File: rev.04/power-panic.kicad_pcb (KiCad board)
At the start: 2 copper layers, 40 x 26 mm, 27 parts, among them P1 PE, P10 AC, P3 N, P5 L, P7 24V, P8 AC_FAULT, P9 measure, Q1 MMBF170LT1G, Q2 MMBF170LT1G, U1 LTV-354T_

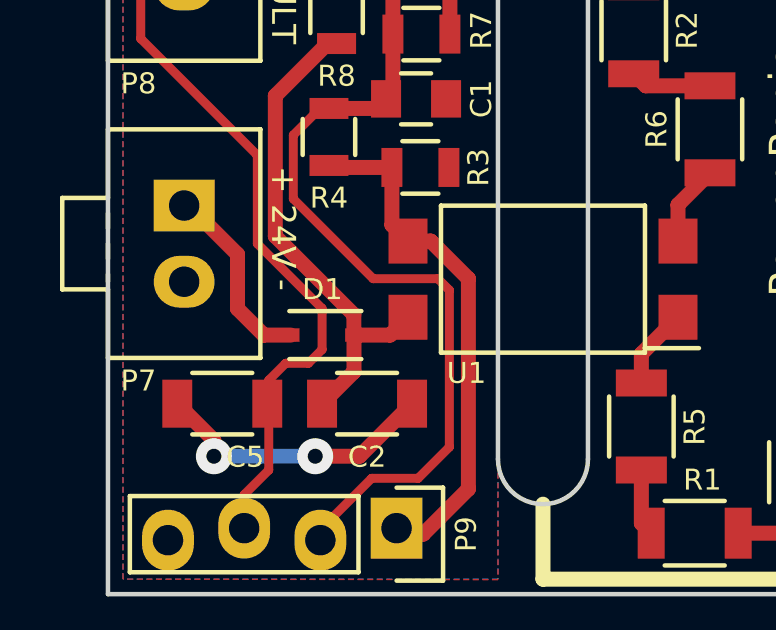
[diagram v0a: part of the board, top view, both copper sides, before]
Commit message: Begin work of reassociating footprints
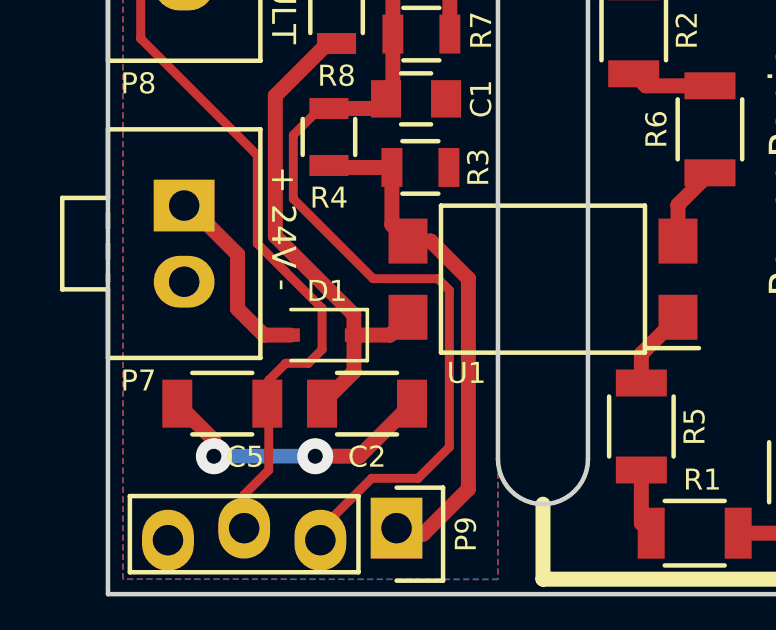
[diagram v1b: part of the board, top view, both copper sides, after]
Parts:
- D1: footprint Diodes_SMD:SOD-323 -> Diodes_SMD:D_SOD-323
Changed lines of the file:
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@@
-(kicad_pcb (version 4) (host pcbnew 4.0.5+dfsg1-4)
+(kicad_pcb (version 4) (host pcbnew 4.0.7)
   (general
     (links 43)
@@
     (43 Eco2.User user)
     (44 Edge.Cuts user)
-    (45 Margin user)
+    (45 Margin user hide)
     (46 B.CrtYd user)
     (47 F.CrtYd user)
@@
     (pad_to_mask_clearance 0.2)
     (aux_axis_origin 0 0)
-    (visible_elements FFFEFF7F)
+    (visible_elements 7FFFFFFF)
     (pcbplotparams
       (layerselection 0x010fc_80000001)
@@
     )
   )
-  (module Diodes_SMD:SOD-323 (layer F.Cu)
-    (at 7.146 -8.636 180)
-    (descr SOD-323)
-    (tags SOD-323)
-    (attr smd)
-    (fp_text reference D1 (at 0 1.524 180) (layer F.SilkS)
-      (effects (font (size 0.7 0.7) (thickness 0.15)))
-    )
-    (fp_text value D_ALT (at 0.1 1.9 180) (layer F.Fab)
-      (effects (font (size 1 1) (thickness 0.15)))
-    )
-    (fp_line (start 0.2 0) (end 0.45 0) (layer F.Fab) (width 0.15))
-    (fp_line (start 0.2 0.35) (end -0.3 0) (layer F.Fab) (width 0.15))
-    (fp_line (start 0.2 -0.35) (end 0.2 0.35) (layer F.Fab) (width 0.15))
-    (fp_line (start -0.3 0) (end 0.2 -0.35) (layer F.Fab) (width 0.15))
-    (fp_line (start -0.3 0) (end -0.5 0) (layer F.Fab) (width 0.15))
-    (fp_line (start -0.3 -0.35) (end -0.3 0.35) (layer F.Fab) (width 0.15))
-    (fp_line (start -0.85 0.65) (end -0.85 -0.65) (layer F.Fab) (width 0.15))
-    (fp_line (start 0.85 0.65) (end -0.85 0.65) (layer F.Fab) (width 0.15))
-    (fp_line (start 0.85 -0.65) (end 0.85 0.65) (layer F.Fab) (width 0.15))
-    (fp_line (start -0.85 -0.65) (end 0.85 -0.65) (layer F.Fab) (width 0.15))
-    (fp_line (start -1.5 -0.95) (end 1.5 -0.95) (layer F.CrtYd) (width 0.05))
-    (fp_line (start 1.5 -0.95) (end 1.5 0.95) (layer F.CrtYd) (width 0.05))
-    (fp_line (start -1.5 0.95) (end 1.5 0.95) (layer F.CrtYd) (width 0.05))
-    (fp_line (start -1.5 -0.95) (end -1.5 0.95) (layer F.CrtYd) (width 0.05))
-    (fp_line (start -1.3 0.8) (end 1.1 0.8) (layer F.SilkS) (width 0.15))
-    (fp_line (start -1.3 -0.8) (end 1.1 -0.8) (layer F.SilkS) (width 0.15))
-    (pad 1 smd rect (at -1.055 0 180) (size 0.59 0.45) (layers F.Cu F.Paste F.Mask)
-      (net 11 /+24V))
-    (pad 2 smd rect (at 1.055 0 180) (size 0.59 0.45) (layers F.Cu F.Paste F.Mask)
-      (net 8 "Net-(D1-Pad2)"))
-    (model Diodes_SMD.3dshapes/SOD-323.wrl
-      (at (xyz 0 0 0))
-      (scale (xyz 1 1 1))
-      (rotate (xyz 0 0 180))
-    )
-  )
   (module Resistors_SMD:R_1206 (layer F.Cu)
     (at 25.146 -7.62 180)
@@
     )
   )
+  (module Diodes_SMD:D_SOD-323 (layer F.Cu)
+    (at 7.146 -8.636 180)
+    (descr SOD-323)
+    (tags SOD-323)
+    (attr smd)
+    (fp_text reference D1 (at -0.154 1.464 180) (layer F.SilkS)
+      (effects (font (size 0.7 0.7) (thickness 0.15)))
+    )
+    (fp_text value D_ALT (at 0.046 1.964 180) (layer F.Fab) hide
+      (effects (font (size 1 1) (thickness 0.15)))
+    )
+    (fp_text user %R (at -0.154 1.464 180) (layer F.Fab) hide
+      (effects (font (size 1 1) (thickness 0.15)))
+    )
+    (fp_line (start -1.5 -0.85) (end -1.5 0.85) (layer F.SilkS) (width 0.12))
+    (fp_line (start 0.2 0) (end 0.45 0) (layer F.Fab) (width 0.1))
+    (fp_line (start 0.2 0.35) (end -0.3 0) (layer F.Fab) (width 0.1))
+    (fp_line (start 0.2 -0.35) (end 0.2 0.35) (layer F.Fab) (width 0.1))
+    (fp_line (start -0.3 0) (end 0.2 -0.35) (layer F.Fab) (width 0.1))
+    (fp_line (start -0.3 0) (end -0.5 0) (layer F.Fab) (width 0.1))
+    (fp_line (start -0.3 -0.35) (end -0.3 0.35) (layer F.Fab) (width 0.1))
+    (fp_line (start -0.9 0.7) (end -0.9 -0.7) (layer F.Fab) (width 0.1))
+    (fp_line (start 0.9 0.7) (end -0.9 0.7) (layer F.Fab) (width 0.1))
+    (fp_line (start 0.9 -0.7) (end 0.9 0.7) (layer F.Fab) (width 0.1))
+    (fp_line (start -0.9 -0.7) (end 0.9 -0.7) (layer F.Fab) (width 0.1))
+    (fp_line (start -1.6 -0.95) (end 1.6 -0.95) (layer F.CrtYd) (width 0.05))
+    (fp_line (start 1.6 -0.95) (end 1.6 0.95) (layer F.CrtYd) (width 0.05))
+    (fp_line (start -1.6 0.95) (end 1.6 0.95) (layer F.CrtYd) (width 0.05))
+    (fp_line (start -1.6 -0.95) (end -1.6 0.95) (layer F.CrtYd) (width 0.05))
+    (fp_line (start -1.5 0.85) (end 1.05 0.85) (layer F.SilkS) (width 0.12))
+    (fp_line (start -1.5 -0.85) (end 1.05 -0.85) (layer F.SilkS) (width 0.12))
+    (pad 1 smd rect (at -1.05 0 180) (size 0.6 0.45) (layers F.Cu F.Paste F.Mask)
+      (net 11 /+24V))
+    (pad 2 smd rect (at 1.05 0 180) (size 0.6 0.45) (layers F.Cu F.Paste F.Mask)
+      (net 8 "Net-(D1-Pad2)"))
+    (model ${KISYS3DMOD}/Diodes_SMD.3dshapes/D_SOD-323.wrl
+      (at (xyz 0 0 0))
+      (scale (xyz 1 1 1))
+      (rotate (xyz 0 0 0))
+    )
+  )
